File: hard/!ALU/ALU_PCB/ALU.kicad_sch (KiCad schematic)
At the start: 37 parts, among them J1 Conn_01x09_Male, J11 Conn_01x01_Male, J12 Conn_01x01_Male, J13 Conn_01x01_Male, J14 Conn_01x01_Male, J2 Conn_01x09_Male, J25 Conn_01x01_Male, J26 Conn_01x01_Male, J27 Conn_01x01_Male, J28 Conn_01x01_Male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

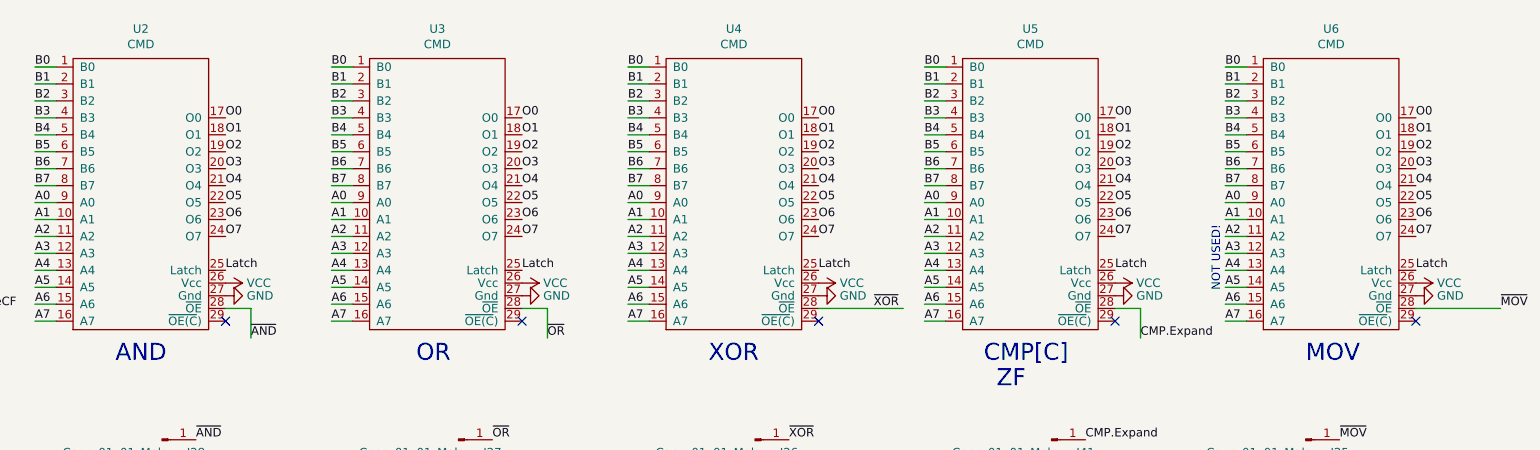
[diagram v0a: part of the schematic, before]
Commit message: Replace AND/OR/XOR/MOV on proper symbol
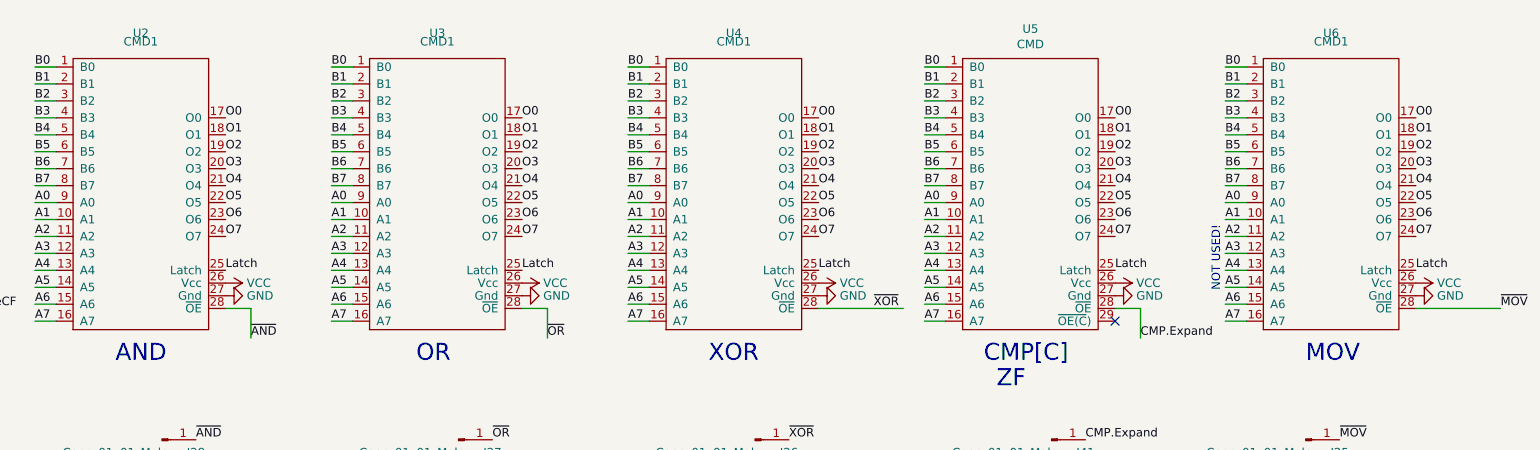
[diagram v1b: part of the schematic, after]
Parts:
- removed U2, U3, U4, U6: CMD, CommonLibrary:CMD, symbol CommonLibrary:CMD
- added U2, U3, U4, U6: CMD1, Common:CMDwoC, symbol Common:CMD1
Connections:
- net A0: now also U2.9 (A0), U3.9 (A0), U4.9 (A0), U6.9 (A0)
- net A1: now also U2.10 (A1), U3.10 (A1), U4.10 (A1), U6.10 (A1)
- net A2: now also U2.11 (A2), U3.11 (A2), U4.11 (A2), U6.11 (A2)
- net A3: now also U2.12 (A3), U3.12 (A3), U4.12 (A3), U6.12 (A3)
- net A4: now also U2.13 (A4), U3.13 (A4), U4.13 (A4), U6.13 (A4)
- net A5: now also U2.14 (A5), U3.14 (A5), U4.14 (A5), U6.14 (A5)
- net A6: now also U2.15 (A6), U3.15 (A6), U4.15 (A6), U6.15 (A6)
- net A7: now also U2.16 (A7), U3.16 (A7), U4.16 (A7), U6.16 (A7)
- net B0: now also U2.1 (B0), U3.1 (B0), U4.1 (B0), U6.1 (B0)
- net B1: now also U2.2 (B1), U3.2 (B1), U4.2 (B1), U6.2 (B1)
- net B2: now also U2.3 (B2), U3.3 (B2), U4.3 (B2), U6.3 (B2)
- net B3: now also U2.4 (B3), U3.4 (B3), U4.4 (B3), U6.4 (B3)
- net B4: now also U2.5 (B4), U3.5 (B4), U4.5 (B4), U6.5 (B4)
- net B5: now also U2.6 (B5), U3.6 (B5), U4.6 (B5), U6.6 (B5)
- net B6: now also U2.7 (B6), U3.7 (B6), U4.7 (B6), U6.7 (B6)
- net B7: now also U2.8 (B7), U3.8 (B7), U4.8 (B7), U6.8 (B7)
- net GND: now also U2.27 (Gnd), U3.27 (Gnd), U4.27 (Gnd), U6.27 (Gnd)
- net Latch: now also U2.25 (Latch), U3.25 (Latch), U4.25 (Latch), U6.25 (Latch)
- net O0: now also U2.17 (O0), U3.17 (O0), U4.17 (O0), U6.17 (O0)
- net O1: now also U2.18 (O1), U3.18 (O1), U4.18 (O1), U6.18 (O1)
- net O2: now also U2.19 (O2), U3.19 (O2), U4.19 (O2), U6.19 (O2)
- net O3: now also U2.20 (O3), U3.20 (O3), U4.20 (O3), U6.20 (O3)
- net O4: now also U2.21 (O4), U3.21 (O4), U4.21 (O4), U6.21 (O4)
- net O5: now also U2.22 (O5), U3.22 (O5), U4.22 (O5), U6.22 (O5)
- net O6: now also U2.23 (O6), U3.23 (O6), U4.23 (O6), U6.23 (O6)
- net O7: now also U2.24 (O7), U3.24 (O7), U4.24 (O7), U6.24 (O7)
- net VCC: now also U2.26 (Vcc), U3.26 (Vcc), U4.26 (Vcc), U6.26 (Vcc)
- net ~{AND}: now also U2.28 (~{OE})
- net ~{MOV}: now also U6.28 (~{OE})
- net ~{OR}: now also U3.28 (~{OE})
- net ~{XOR}: now also U4.28 (~{OE})
- no-connect marks 7 -> 3
